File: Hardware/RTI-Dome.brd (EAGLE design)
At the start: 80 x 71.1 mm, 32 parts, among them IC2 74LVC244

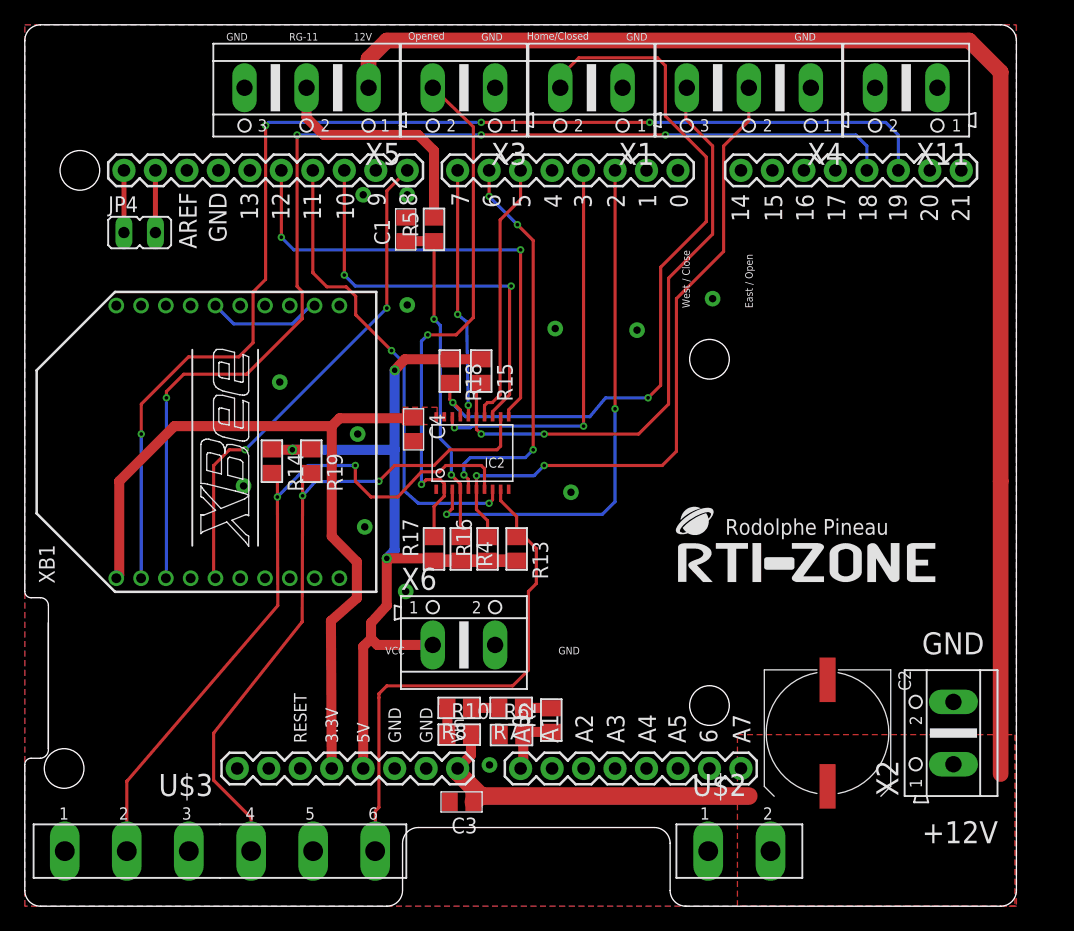
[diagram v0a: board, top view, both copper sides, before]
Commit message: Auto detect shutter presence.
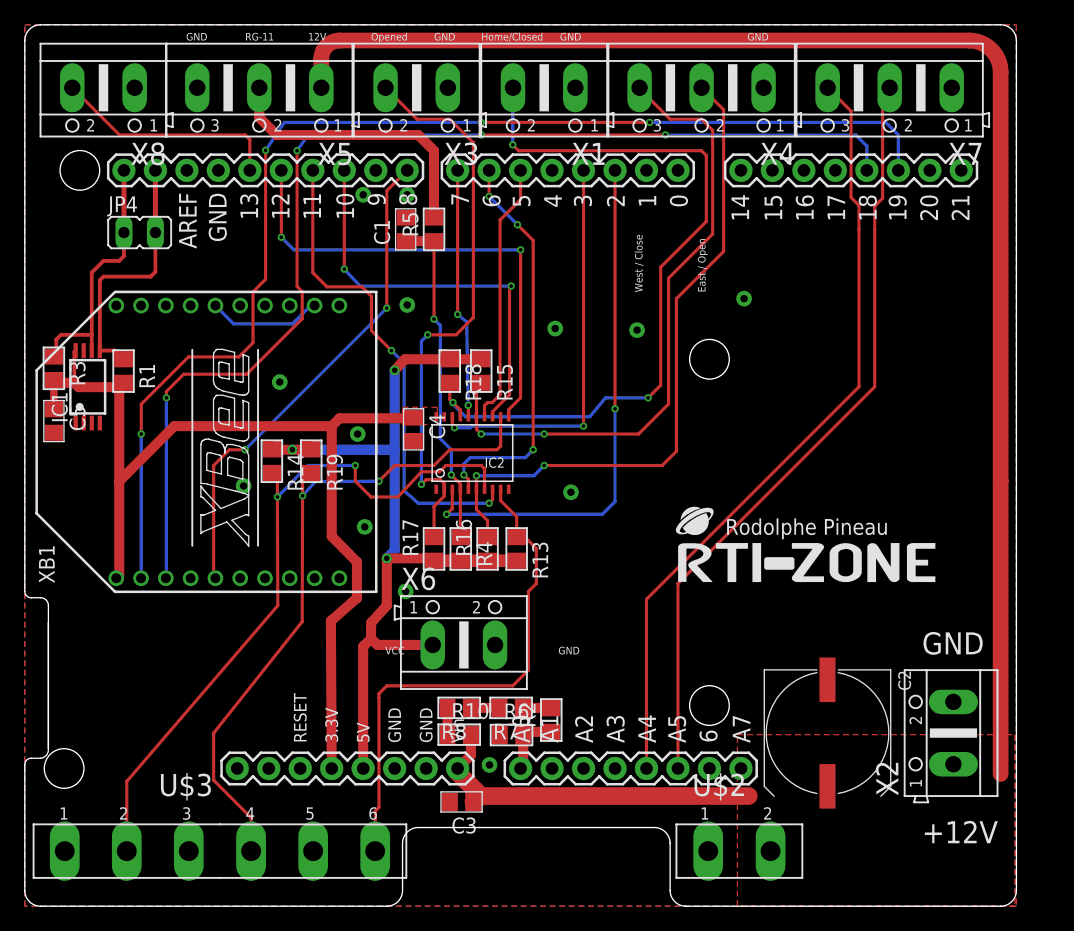
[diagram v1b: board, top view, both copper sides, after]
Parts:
- removed X11: (no value), con-ptr500:AK500/2
- added C5: 100nF, rti:C0805
- added IC1: 24AA128ST, microchip:TSSOP8
- added R1, R3: 1K, rti:R0805
- added X7: (no value), con-ptr500:AK500/3
- added X8: (no value), con-ptr500:AK500/2
- moved X1 3.81 mm to (41.9, 66.0)
- moved X4 3.81 mm to (54.6, 66.0)
- moved X5 3.81 mm to (18.9, 66.0)
- moved X3 3.81 mm to (31.6, 66.0)
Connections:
- removed net N$6: JP4.1, PCB1.SCL1
- removed net N$8: JP4.2, PCB1.SDA1
- new net SCL: IC1.6, JP4.1, PCB1.SCL1, R3.1
- new net SDA: IC1.5, JP4.2, PCB1.SDA1, R1.1
- net 13: now also X8.2
- net 3.3V: now also C5.1, IC1.8, R1.2, R3.2
- net AT_PARK_PIN: now also X7.2; no longer X11.1
- net AT_PARK_PIN_LOOP: now also X7.3; no longer X11.2
- net GND: now also C5.2, IC1.1, IC1.2, IC1.3, IC1.4, X7.1, X8.1
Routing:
- net AT_PARK_PIN_LOOP: track 0.00 -> 63.1 mm
- net AT_PARK_PIN: track 0.00 -> 62.0 mm
- net SDA: track 0.00 -> 20.8 mm
- net SCL: track 0.00 -> 20.8 mm
- net 3.3V: track 63.3 -> 81.9 mm
- net 13: track 0.00 -> 18.5 mm
- net N$8: track 5.02 -> 0.00 mm
- net N$6: track 5.02 -> 0.00 mm
- net RG-11-IN_EXT: track 19.2 -> 23.0 mm
- net +12V: track 140.2 -> 144.0 mm
- net BUTTON_WEST_CLOSE_5V: track 48.4 -> 51.5 mm
- net SHUTTER_OPENED_5V: track 43.3 -> 46.4 mm
- net HOME_SHUTTER_CLOSED_5V: track 60.5 -> 62.2 mm, vias 2 -> 3
- net XBEE_DOUT: track 97.5 -> 96.6 mm
- net M_DIR: track 38.3 -> 39.0 mm
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
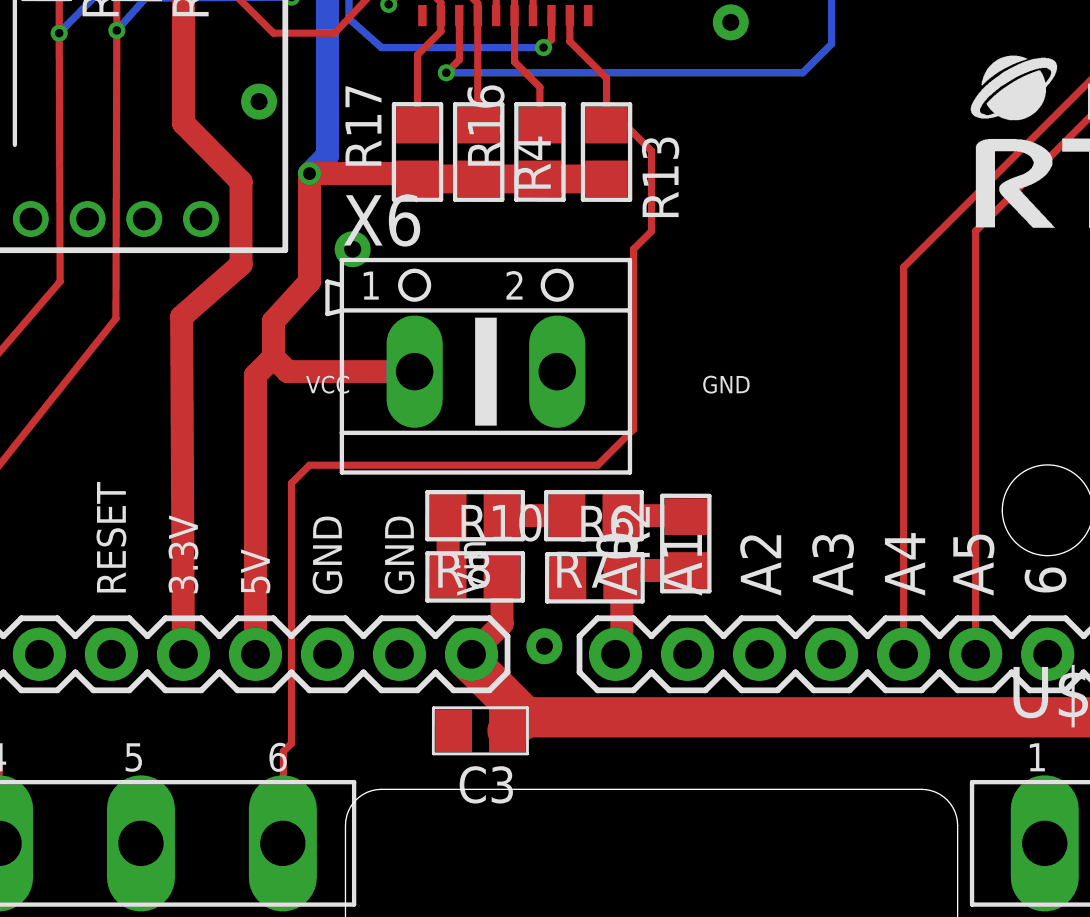
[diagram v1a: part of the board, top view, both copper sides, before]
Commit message: Tested the ISD04 stepper controller.. needed to add 3.3V header as the pull-up on the buffer output don't bring the signal to 5V and therefore the optocoupler in the contoller doesn't do the right thing.
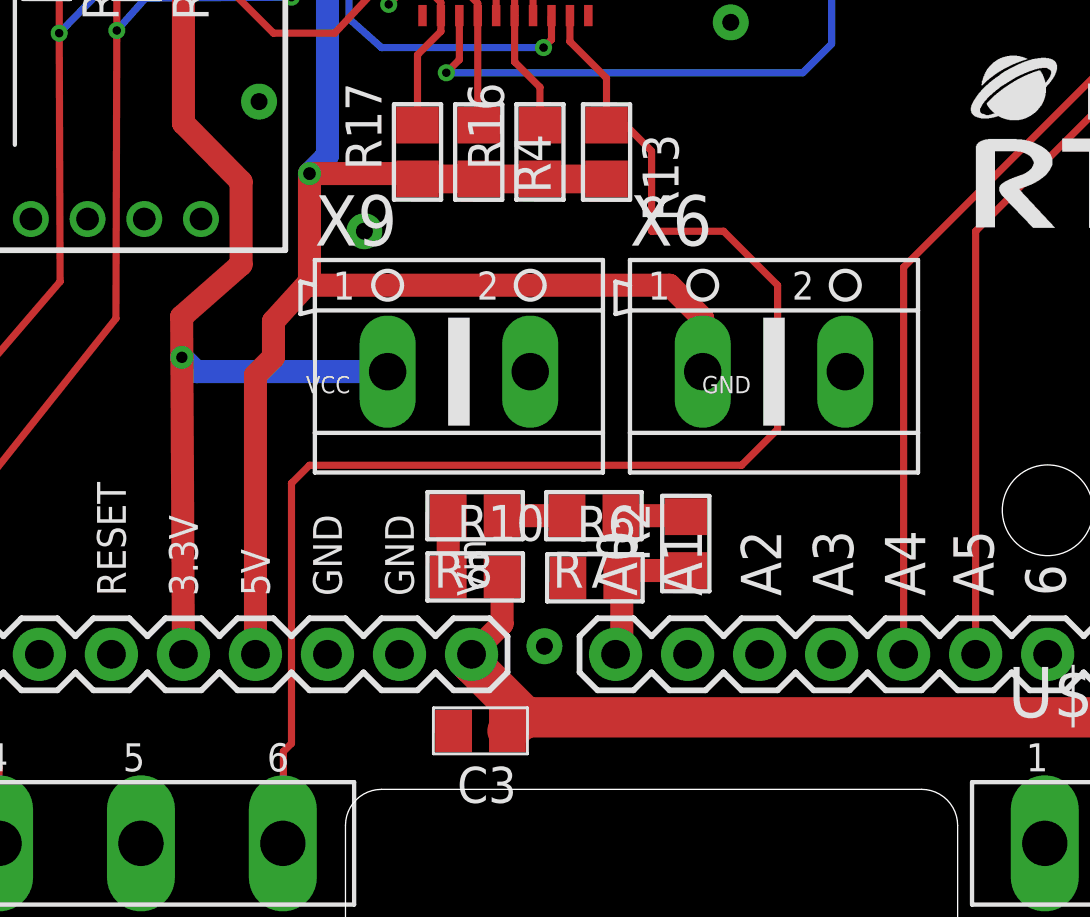
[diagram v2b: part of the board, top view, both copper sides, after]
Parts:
- added X9: (no value), con-ptr500:AK500/2
- moved X6 10.2 mm to (45.6, 21.1)
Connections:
- net 3.3V: now also X9.1
- net GND: now also X9.2
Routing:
- net VCC: track 67.7 -> 78.8 mm
- net M_STEP_5V: track 42.1 -> 50.3 mm
- net 3.3V: track 81.9 -> 89.3 mm, vias 0 -> 1
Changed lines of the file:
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@@
 <attribute name="OC_NEWARK" value="34R5507" x="16.383" y="37.465" size="1.778" layer="27" rot="R90" display="off"/>
 </element>
-<element name="X6" library="con-ptr500" package="AK500/2" value="" x="35.433" y="21.082">
-<attribute name="OC_FARNELL" value="unknown" x="35.433" y="21.082" size="1.778" layer="27" display="off"/>
-<attribute name="MF" value="" x="35.433" y="21.082" size="1.778" layer="27" display="off"/>
-<attribute name="MPN" value="" x="35.433" y="21.082" size="1.778" layer="27" display="off"/>
-<attribute name="OC_NEWARK" value="unknown" x="35.433" y="21.082" size="1.778" layer="27" display="off"/>
+<element name="X6" library="con-ptr500" package="AK500/2" value="" x="45.593" y="21.082">
+<attribute name="OC_FARNELL" value="unknown" x="45.593" y="21.082" size="1.778" layer="27" display="off"/>
+<attribute name="MF" value="" x="45.593" y="21.082" size="1.778" layer="27" display="off"/>
+<attribute name="MPN" value="" x="45.593" y="21.082" size="1.778" layer="27" display="off"/>
+<attribute name="OC_NEWARK" value="unknown" x="45.593" y="21.082" size="1.778" layer="27" display="off"/>
 </element>
 <element name="PCB1" library="arduino_shield" package="ARDUINO_DUE_SHIELD_SHORT" value="ARDUINO_DUE_SHIELD_SHORT" x="40.005" y="32.7025"/>
@@
 <element name="R3" library="rti" package="R0805" value="1K" x="2.3495" y="43.40225" rot="R270"/>
 <element name="C5" library="rti" package="C0805" value="100nF" x="2.3495" y="39.14775" rot="R270"/>
+<element name="X9" library="con-ptr500" package="AK500/2" value="" x="34.4805" y="21.082">
+<attribute name="OC_NEWARK" value="unknown" x="34.4805" y="21.082" size="1.778" layer="27" display="off"/>
+<attribute name="OC_FARNELL" value="unknown" x="34.4805" y="21.082" size="1.778" layer="27" display="off"/>
+<attribute name="MF" value="" x="34.4805" y="21.082" size="1.778" layer="27" display="off"/>
+<attribute name="MPN" value="" x="34.4805" y="21.082" size="1.778" layer="27" display="off"/>
+</element>
 </elements>
 <signals>
@@
 <via x="26.8605" y="38.1" extent="1-16" drill="0.6" diameter="1.27"/>
 <via x="42.799" y="46.609" extent="1-16" drill="0.6" diameter="1.27"/>
-<via x="30.734" y="25.4" extent="1-16" drill="0.6" diameter="1.27"/>
+<via x="31.14675" y="26.035" extent="1-16" drill="0.6" diameter="1.27"/>
 <via x="27.432" y="30.607" extent="1-16" drill="0.6" diameter="1.27"/>
 <contactref element="XB1" pad="9"/>
@@
 <contactref element="IC1" pad="1"/>
 <contactref element="C5" pad="2"/>
+<contactref element="X9" pad="2"/>
 </signal>
 <signal name="+12V" class="1">
@@
 <wire x1="7.62" y1="26.702" x2="7.383" y2="26.465" width="0.8128" layer="1"/>
 <contactref element="PCB1" pad="3.3V"/>
-<wire x1="24.765" y1="11.1125" x2="24.7015" y2="23.01875" width="0.8128" layer="1"/>
+<wire x1="24.765" y1="11.1125" x2="24.709140625" y2="21.586315625" width="0.8128" layer="1"/>
+<wire x1="24.709140625" y1="21.586315625" x2="24.709103125" y2="21.5930875" width="0.8128" layer="1"/>
+<wire x1="24.709103125" y1="21.5930875" x2="24.7015" y2="23.01875" width="0.8128" layer="1"/>
 <wire x1="24.7015" y1="23.01875" x2="26.797" y2="24.86025" width="0.8128" layer="1"/>
 <wire x1="26.797" y1="24.86025" x2="26.797" y2="27.78125" width="0.8128" layer="1"/>
@@
 <wire x1="2.3495" y1="40.09775" x2="2.3495" y2="42.38875" width="0.6096" layer="1"/>
 <wire x1="2.3495" y1="42.38875" x2="2.3495" y2="42.45225" width="0.6096" layer="1"/>
+<contactref element="X9" pad="1"/>
+<wire x1="31.9659" y1="21.082" x2="25.21345625" y2="21.082" width="0.8128" layer="16"/>
+<wire x1="25.21345625" y1="21.082" x2="24.709140625" y2="21.586315625" width="0.8128" layer="16"/>
+<via x="24.709140625" y="21.586315625" extent="1-16" drill="0.4" diameter="0.8128"/>
+<wire x1="24.709140625" y1="21.586315625" x2="24.709140625" y2="21.59305" width="0.8128" layer="1"/>
 <wire x1="4.09575" y1="44.82575" x2="4.105" y2="44.835" width="0" layer="19" extent="1-1"/>
 </signal>
@@
 <contactref element="IC2" pad="P$9"/>
 <wire x1="38.395" y1="33.64" x2="38.395" y2="32.725" width="0.254" layer="1"/>
-<wire x1="28.575" y1="10.4775" x2="28.575" y2="16.8275" width="0.254" layer="1"/>
-<wire x1="28.575" y1="16.8275" x2="28.575" y2="17.145" width="0.254" layer="1"/>
+<wire x1="28.575" y1="7.96925" x2="28.575" y2="17.145" width="0.254" layer="1"/>
 <wire x1="28.575" y1="17.145" x2="29.21" y2="17.78" width="0.254" layer="1"/>
-<wire x1="29.21" y1="17.78" x2="39.37" y2="17.78" width="0.254" layer="1"/>
-<wire x1="39.37" y1="17.78" x2="40.64" y2="19.05" width="0.254" layer="1"/>
-<wire x1="40.64" y1="19.05" x2="40.64" y2="25.4" width="0.254" layer="1"/>
+<wire x1="29.21" y1="17.78" x2="44.45" y2="17.78" width="0.254" layer="1"/>
+<wire x1="44.45" y1="17.78" x2="45.72" y2="19.05" width="0.254" layer="1"/>
+<wire x1="45.72" y1="19.05" x2="45.72" y2="24.13" width="0.254" layer="1"/>
 <wire x1="38.395" y1="32.725" x2="39.6875" y2="31.4325" width="0.254" layer="1"/>
 <wire x1="39.6875" y1="31.4325" x2="39.6875" y2="29.779" width="0.254" layer="1"/>
@@
 <wire x1="40.35675" y1="29.779" x2="41.275" y2="28.86075" width="0.254" layer="1"/>
 <wire x1="41.275" y1="28.86075" x2="41.275" y2="26.035" width="0.254" layer="1"/>
-<wire x1="41.275" y1="26.035" x2="40.64" y2="25.4" width="0.254" layer="1"/>
-<wire x1="28.575" y1="10.4775" x2="28.575" y2="7.96925" width="0.254" layer="1"/>
+<wire x1="41.275" y1="26.035" x2="43.815" y2="26.035" width="0.254" layer="1"/>
+<wire x1="43.815" y1="26.035" x2="45.72" y2="24.13" width="0.254" layer="1"/>
 <wire x1="28.575" y1="7.96925" x2="28.28925" y2="7.6835" width="0.254" layer="1"/>
 <wire x1="28.28925" y1="7.6835" x2="28.28925" y2="4.46405" width="0.254" layer="1"/>
@@
 <wire x1="27.305" y1="20.955" x2="27.94" y2="21.59" width="0.8128" layer="1"/>
 <wire x1="27.94" y1="21.59" x2="27.94" y2="22.86" width="0.8128" layer="1"/>
-<wire x1="27.94" y1="22.86" x2="29.21" y2="24.257" width="0.8128" layer="1"/>
+<wire x1="27.94" y1="22.86" x2="29.1467875" y2="24.187465625" width="0.8128" layer="1"/>
+<wire x1="29.1467875" y1="24.187465625" x2="29.21" y2="24.257" width="0.8128" layer="1"/>
 <wire x1="29.21" y1="24.257" x2="29.21" y2="28.067" width="0.8128" layer="1"/>
 <wire x1="29.21" y1="28.067" x2="32.832" y2="28.067" width="0.8128" layer="1"/>
@@
 <contactref element="X6" pad="1"/>
 <contactref element="PCB1" pad="5V"/>
-<wire x1="32.9184" y1="21.082" x2="28.448" y2="21.082" width="0.8128" layer="1"/>
-<wire x1="28.448" y1="21.082" x2="27.94" y2="21.59" width="0.8128" layer="1"/>
 <wire x1="39.6875" y1="27.879" x2="37.338" y2="27.879" width="1.016" layer="1"/>
 <wire x1="23.114" y1="36.85925" x2="23.08475" y2="36.83" width="0.4064" layer="1"/>
@@
 <wire x1="19.939" y1="36.85925" x2="19.96825" y2="36.83" width="0.4064" layer="1"/>
 <wire x1="19.96825" y1="36.83" x2="21.59" y2="36.83" width="0.8128" layer="1"/>
+<wire x1="43.0784" y1="21.082" x2="43.0784" y2="22.9616" width="0.8128" layer="1"/>
+<wire x1="43.0784" y1="22.9616" x2="41.91" y2="24.13" width="0.8128" layer="1"/>
+<wire x1="41.91" y1="24.13" x2="29.204253125" y2="24.13" width="0.8128" layer="1"/>
+<wire x1="29.204253125" y1="24.13" x2="29.1467875" y2="24.187465625" width="0.8128" layer="1"/>
 </signal>
 <signal name="N$2">

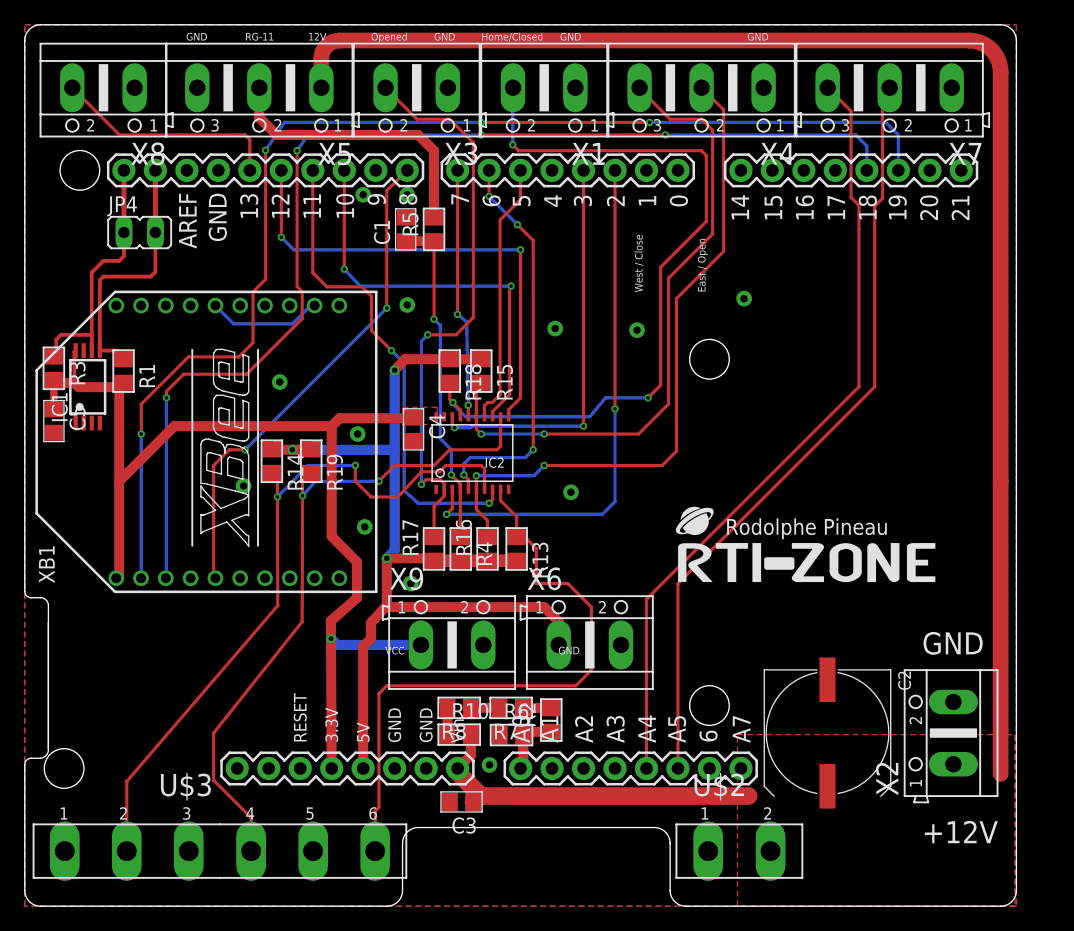
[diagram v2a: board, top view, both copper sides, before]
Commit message: Adding a usb-serial + usb port on SERIAL2 (pin 16 and 17)
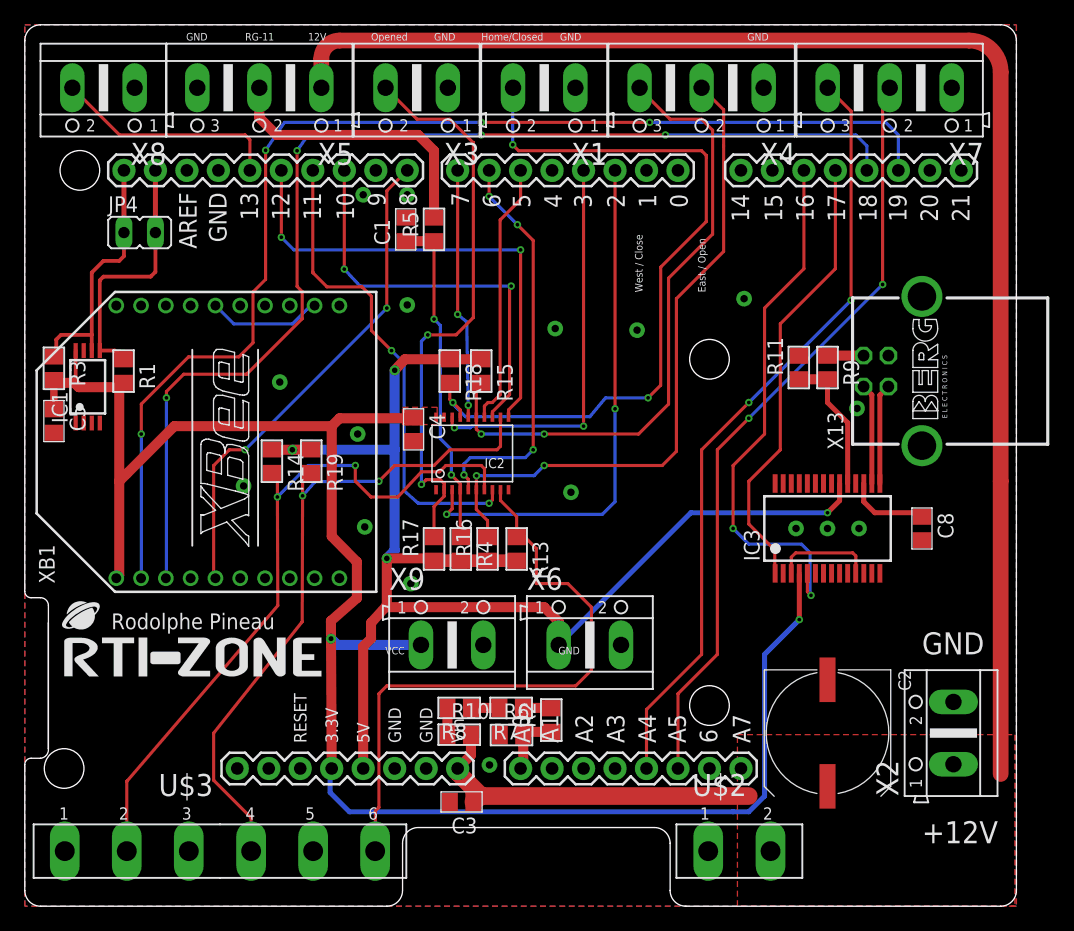
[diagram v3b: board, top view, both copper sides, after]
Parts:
- added C8: 100nF, rti:C0805
- added IC3: FT232RL, ftdichip:SSOP28
- added R11: 10K, rti:R0805
- added R9: 4.7K, rti:R0805
- added X13: PN61729-S, con-berg:PN61729-S
- moved U$4 50.1 mm to (3.17, 18.5)
- moved IC2 0.81 mm to (36.1, 36.5)
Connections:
- new net N$1: IC3.19, R11.1, R9.2
- new net N$21: IC3.10
- new net N$4: IC3.11, IC3.3
- new net N$6: C8.1, IC3.17
- new net RX2: IC3.1, PCB1.17
- new net TX2: IC3.5, PCB1.16
- new net USBDM: IC3.16, X13.2
- new net USBDP: IC3.15, X13.3
- new net USB_VCC: R9.1, X13.1
- net 3.3V: now also IC3.4
- net GND: now also C8.2, IC3.18, IC3.21, IC3.25, IC3.7, R11.2, X13.4, X13.S1, X13.S2
- net VCC: now also IC3.20
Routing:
- net 3.3V: track 89.3 -> 146.7 mm, vias 1 -> 2
- net TX2: track 0.00 -> 43.6 mm, vias 0 -> 2
- net RX2: track 0.00 -> 36.3 mm
- net VCC: track 78.8 -> 107.7 mm, vias 3 -> 4
- net N$1: track 0.00 -> 11.4 mm
- net N$4: track 0.00 -> 8.17 mm
- net USBDP: track 0.00 -> 8.11 mm
- net USBDM: track 0.00 -> 8.10 mm
- net N$6: track 0.00 -> 6.66 mm
- net USB_VCC: track 0.00 -> 2.92 mm
- net AT_PARK_PIN_LOOP: track 63.1 -> 62.5 mm, vias 0 -> 2
- net AT_PARK_PIN: vias 0 -> 2
